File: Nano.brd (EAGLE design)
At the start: 100 x 80 mm, 24 parts

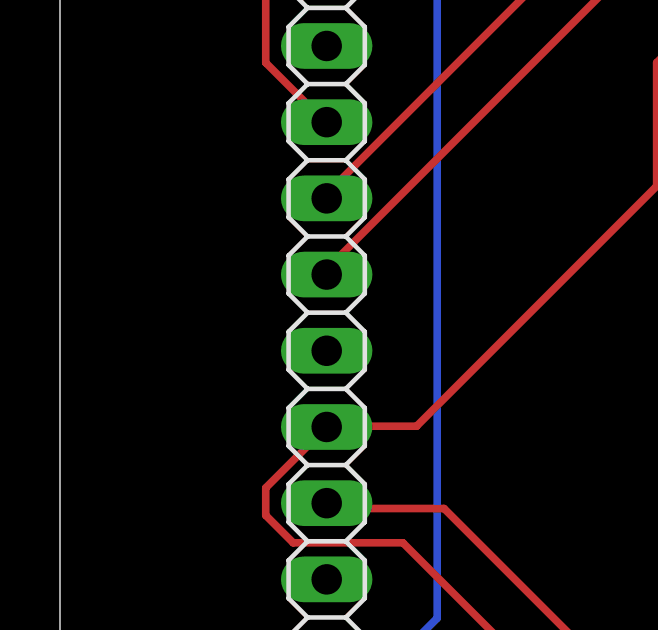
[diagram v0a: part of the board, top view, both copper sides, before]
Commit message: 
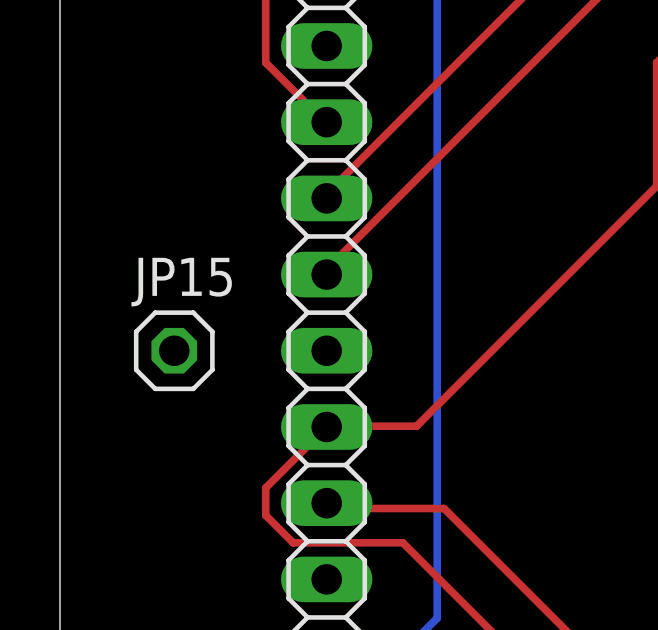
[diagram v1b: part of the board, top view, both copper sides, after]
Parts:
- added JP15: Batt, pinhead:1X01
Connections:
- new net N$6: JP15.1, JP2.9
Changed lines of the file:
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@@
 <?xml version="1.0" encoding="utf-8"?>
 <!DOCTYPE eagle SYSTEM "eagle.dtd">
-<eagle version="7.7.0">
+<eagle version="8.5.1">
 <drawing>
 <settings>
 <setting alwaysvectorfont="no"/>
+<setting keepoldvectorfont="yes"/>
 <setting verticaltext="up"/>
 </settings>
@@
 <layer number="223" name="223bmp" color="24" fill="1" visible="no" active="no"/>
 <layer number="224" name="224bmp" color="25" fill="1" visible="no" active="no"/>
+<layer number="225" name="225bmp" color="7" fill="1" visible="yes" active="yes"/>
+<layer number="226" name="226bmp" color="7" fill="1" visible="yes" active="yes"/>
+<layer number="227" name="227bmp" color="7" fill="1" visible="yes" active="yes"/>
+<layer number="228" name="228bmp" color="7" fill="1" visible="yes" active="yes"/>
+<layer number="229" name="229bmp" color="7" fill="1" visible="yes" active="yes"/>
+<layer number="230" name="230bmp" color="7" fill="1" visible="yes" active="yes"/>
 <layer number="231" name="Eagle3D_PG1" color="7" fill="1" visible="no" active="no"/>
 <layer number="232" name="Eagle3D_PG2" color="7" fill="1" visible="no" active="no"/>
@@
 <param name="dpMaxLengthDifference" value="10mm"/>
 <param name="dpGapFactor" value="2.5"/>
-<param name="checkGrid" value="0"/>
 <param name="checkAngle" value="0"/>
 <param name="checkFont" value="1"/>
 <param name="checkRestrict" value="1"/>
+<param name="checkStop" value="0"/>
+<param name="checkValues" value="0"/>
 <param name="useDiameter" value="13"/>
 <param name="maxErrors" value="50"/>
@@
 <element name="JP14" library="SparkFun-Connectors" package="1X02_LOCK" value="I2C" x="54.61" y="7.62"/>
 <element name="JP9" library="SparkFun-Connectors" package="1X07" value="Tast" x="63.5" y="44.45" rot="R270"/>
+<element name="JP15" library="pinhead" package="1X01" value="Batt" x="3.81" y="34.29"/>
 </elements>
 <signals>
@@
 <wire x1="57.15" y1="29.2608" x2="57.15" y2="29.21" width="0.254" layer="1"/>
 </signal>
+<signal name="N$6">
+<contactref element="JP15" pad="1"/>
+<contactref element="JP2" pad="9"/>
+<wire x1="3.81" y1="34.29" x2="8.89" y2="34.29" width="0" layer="19" extent="1-1"/>
+</signal>
 </signals>

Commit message: 
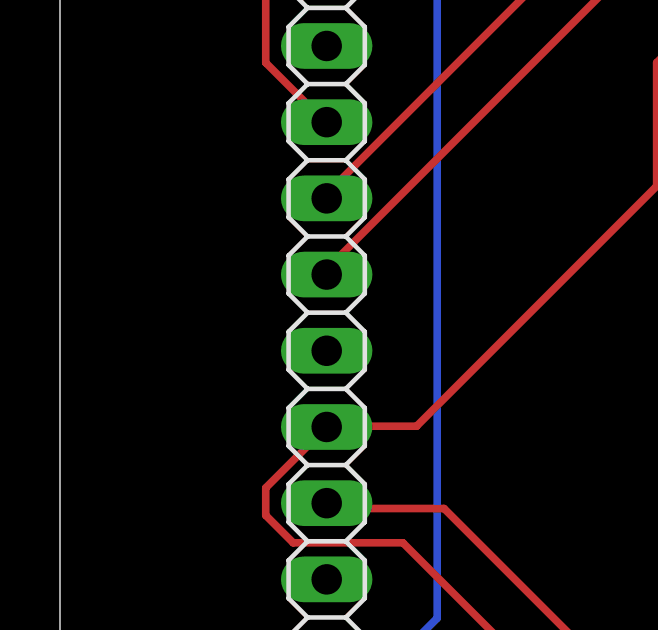
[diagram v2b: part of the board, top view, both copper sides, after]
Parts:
- removed JP15: Batt, pinhead:1X01
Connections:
- removed net N$6: JP15.1, JP2.9
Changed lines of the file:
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@@
 <element name="JP14" library="SparkFun-Connectors" package="1X02_LOCK" value="I2C" x="54.61" y="7.62"/>
 <element name="JP9" library="SparkFun-Connectors" package="1X07" value="Tast" x="63.5" y="44.45" rot="R270"/>
-<element name="JP15" library="pinhead" package="1X01" value="Batt" x="3.81" y="34.29"/>
 </elements>
 <signals>
@@
 <wire x1="57.15" y1="29.2608" x2="57.15" y2="29.21" width="0.254" layer="1"/>
 </signal>
-<signal name="N$6">
-<contactref element="JP15" pad="1"/>
-<contactref element="JP2" pad="9"/>
-<wire x1="3.81" y1="34.29" x2="8.89" y2="34.29" width="0" layer="19" extent="1-1"/>
-</signal>
 </signals>
